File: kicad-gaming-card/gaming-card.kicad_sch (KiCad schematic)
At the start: 81 parts

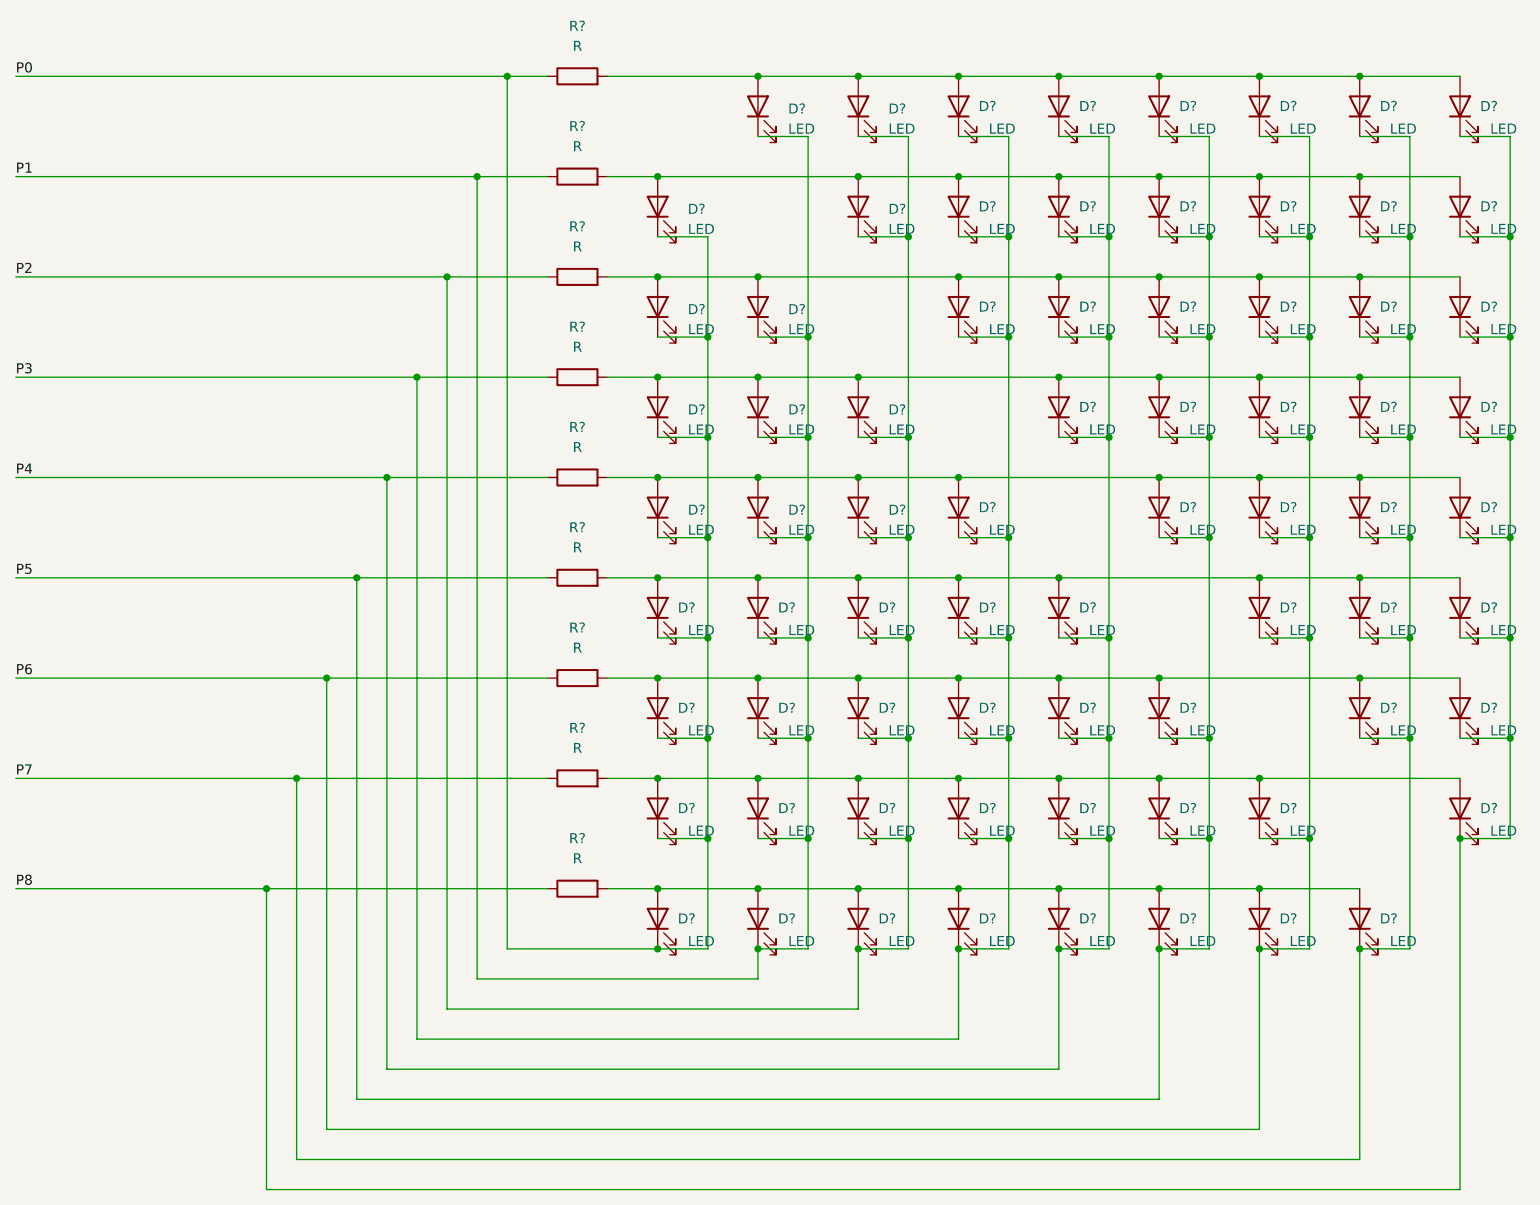
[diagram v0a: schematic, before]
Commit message: update schematic
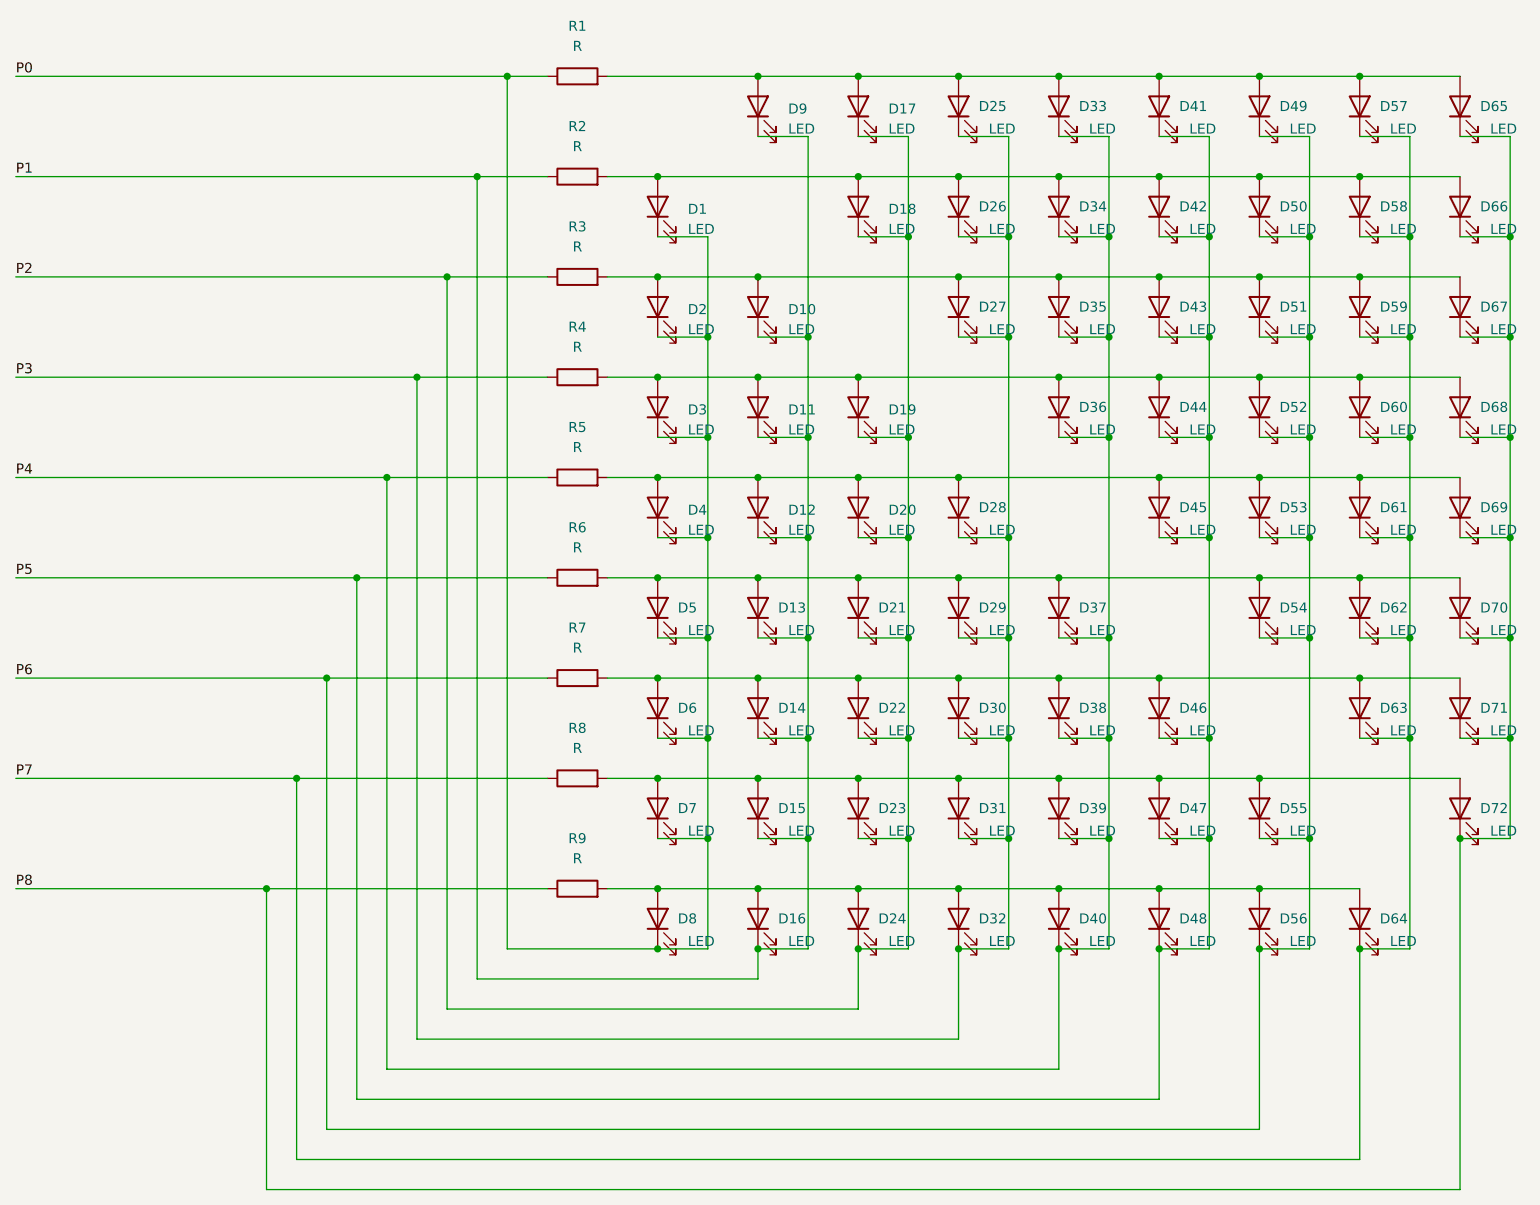
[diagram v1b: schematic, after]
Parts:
- gave numbers to parts that had none: 81
